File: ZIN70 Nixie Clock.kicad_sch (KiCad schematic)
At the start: 28 parts, among them U1 HV5122, U2 HV5122, U3 CD40109BPW, U4 LM78M05_TO220

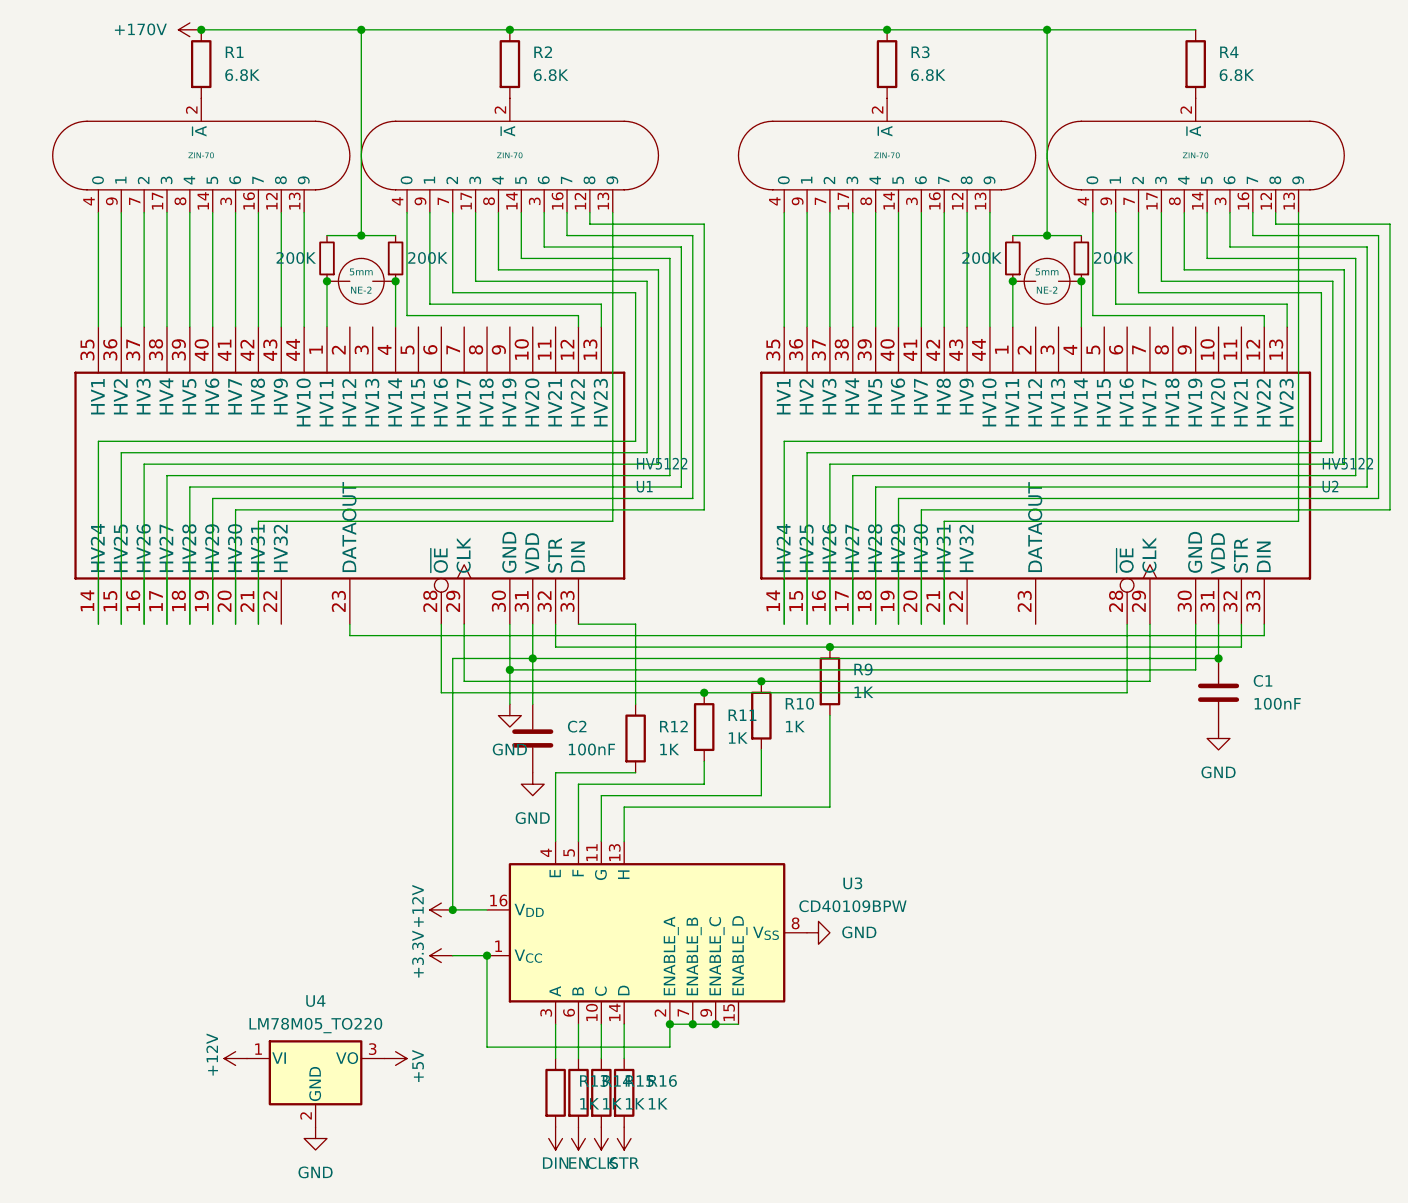
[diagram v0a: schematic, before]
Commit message: Fix all issues, replace some components, simplify / improve design
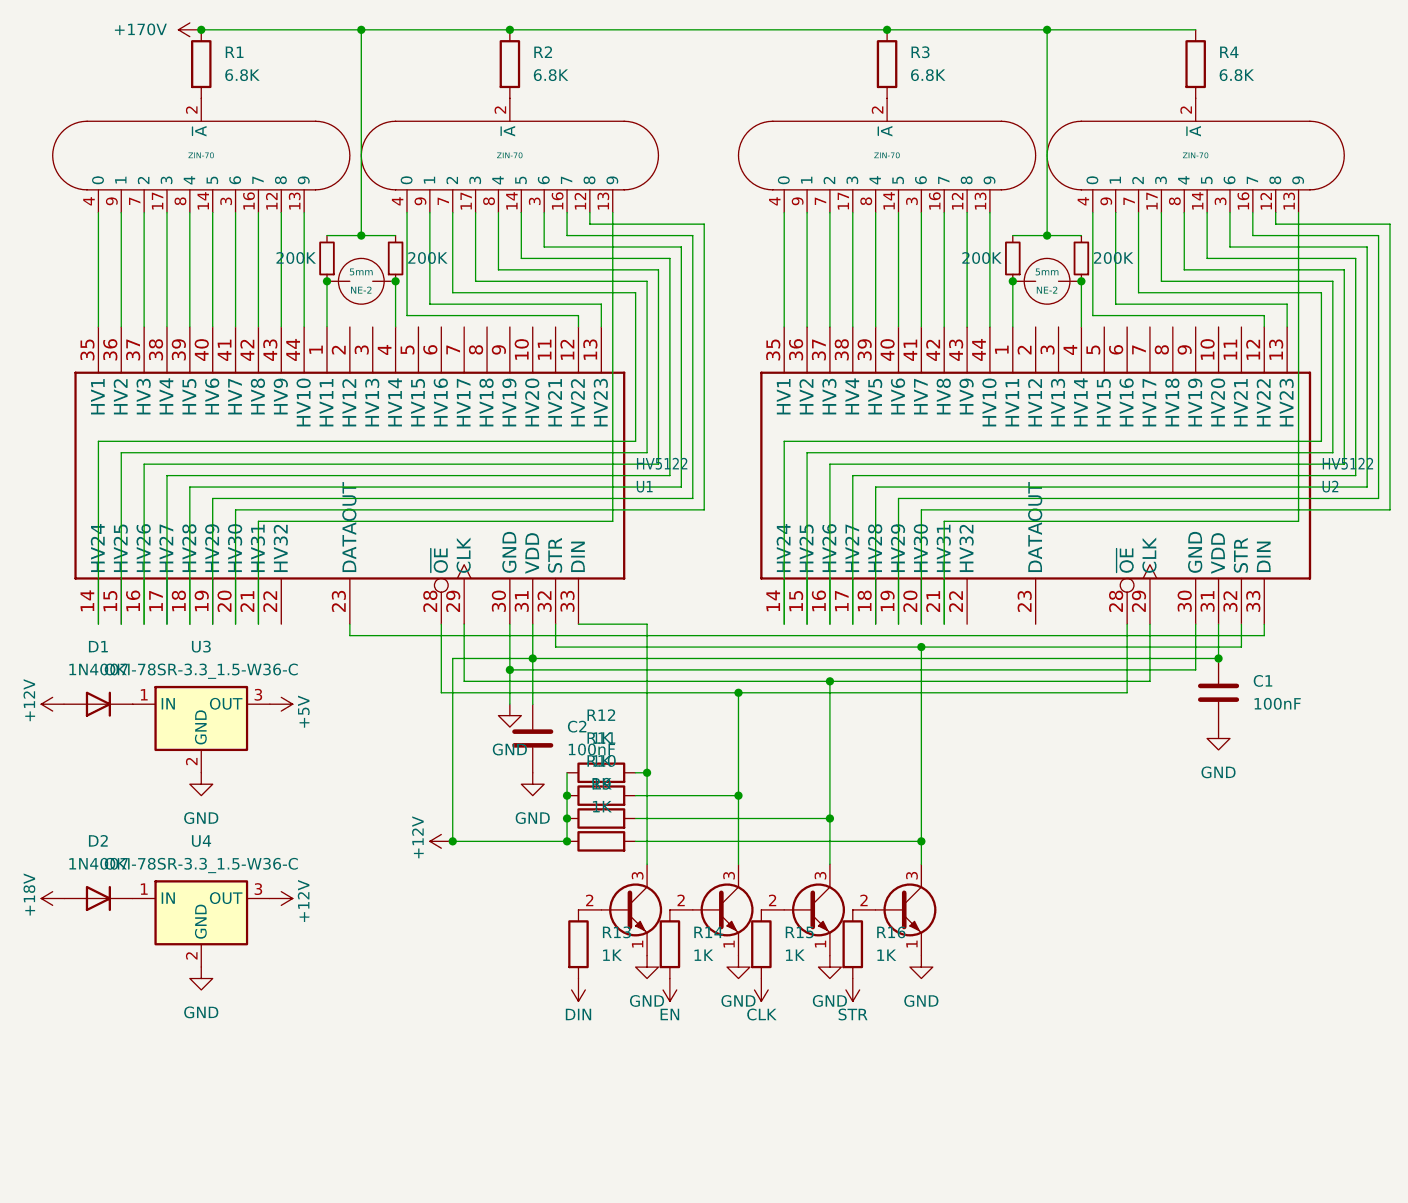
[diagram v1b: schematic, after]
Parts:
- removed U3: CD40109BPW, Package_SO:TSSOP-16_4.4x5mm_P0.65mm, symbol Logic_LevelTranslator:CD40109BPW
- removed U4: LM78M05_TO220, Package_TO_SOT_THT:TO-220-3_Vertical, symbol Regulator_Linear:LM78M05_TO220
- added D1, D2: 1N4007, Diode_THT:D_DO-41_SOD81_P10.16mm_Horizontal, symbol Diode:1N4007
- added Q1, Q2, Q3, Q4: PN2222A, Package_TO_SOT_THT:TO-92_Inline, symbol Transistor_BJT:PN2222A
- added U3, U4: OKI-78SR-3.3_1.5-W36-C, Converter_DCDC:Converter_DCDC_Murata_OKI-78SR_Vertical, symbol Converter_DCDC:OKI-78SR-3.3_1.5-W36-C
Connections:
- net +12V: now also R10.1, R11.1, R12.1, R9.1, D1.2 (A), U4.3 (OUT)
- net +5V: now also U3.3 (OUT)
- net GND: now also Q1.1 (E), Q2.1 (E), Q3.1 (E), Q4.1 (E), U3.2 (GND), U4.2 (GND)
- net at R14.1: now also Q2.2 (B)
- net at U1.28 (~{OE}), U2.28 (~{OE}): now also R11.2, Q2.3 (C); no longer R11.1
- net at U1.29 (CLK), U2.29 (CLK): now also R10.2, Q3.3 (C); no longer R10.1
- net at U1.32 (STR), U2.32 (STR): now also R9.2, Q4.3 (C); no longer R9.1
- net at U1.33 (DIN): now also R12.2, Q1.3 (C); no longer R12.1
- net at R13.1: now also Q1.2 (B)
- net at R15.1: now also Q3.2 (B)
- net at R16.1: now also Q4.2 (B)
- new net: D1.1 (K), U3.1 (IN)
- new net: D2.1 (K), U4.1 (IN)
- new net +18V: D2.2 (A)
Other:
- moved on the sheet: R10, R11, R12, R13, R14, R15, R16, R9
